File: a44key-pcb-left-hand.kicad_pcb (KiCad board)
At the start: 2 copper layers, 116.7 x 103.9 mm, 69 parts, among them J1 AudioJack3, J2 Conn_01x04_Female, J3 Conn_01x04_Female, J4 Conn_01x04_Female, SW1 SW_Push, U1 ATmega32U4-AU, Y1 16MHz

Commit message: PCB Left Hand Added
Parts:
- moved C7 18.9 mm to (180.3, 127.7)
- moved C6 18.9 mm to (175.0, 127.7)
- moved C9 18.9 mm to (173.0, 127.7)
- moved Right-Left1 18.8 mm to (181.6, 108.9), turned to 270 degrees
- moved R4 18.1 mm to (178.3, 109.1)
- moved C8 16.0 mm to (171.6, 110.5)
- moved R3 10.1 mm to (164.9, 122.9)
- moved R5 8.23 mm to (161.3, 121.8)
- moved C2 7.42 mm to (159.5, 114.2)
- moved F1 6.86 mm to (163.1, 56.6), turned to 90 degrees
- moved C4 6.06 mm to (164.9, 120.9)
- moved Y1 4.86 mm to (163.7, 115.2)
- moved C11 3.94 mm to (182.9, 121.0)
- moved R2 3.05 mm to (158.0, 56.4), turned to 90 degrees
- moved C1 1.82 mm to (182.9, 124.7)
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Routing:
- net COL0: track 0.00 -> 260.3 mm, vias 0 -> 4
- net COL1: track 0.00 -> 233.0 mm, vias 0 -> 2
- net COL2: track 0.00 -> 202.1 mm, vias 0 -> 1
- net COL5: track 0.00 -> 184.6 mm, vias 0 -> 1
- net GND: track 0.00 -> 176.1 mm, vias 0 -> 4
- net COL3: track 0.00 -> 173.1 mm
- net COL4: track 0.00 -> 136.2 mm, vias 0 -> 1
- net VCC: track 0.00 -> 136.1 mm, vias 0 -> 5
- net Net-(R2-Pad1): track 0.00 -> 117.1 mm, vias 0 -> 2
- net Net-(R1-Pad1): track 0.00 -> 112.4 mm, vias 0 -> 2
- net +5V: track 0.00 -> 109.1 mm, vias 0 -> 3
- net ROW1: track 0.00 -> 94.5 mm, vias 0 -> 3
- net TH35: track 0.00 -> 89.1 mm, vias 0 -> 2
- net ROW0: track 0.00 -> 77.9 mm, vias 0 -> 2
- net SCL: track 0.00 -> 76.7 mm, vias 0 -> 2
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
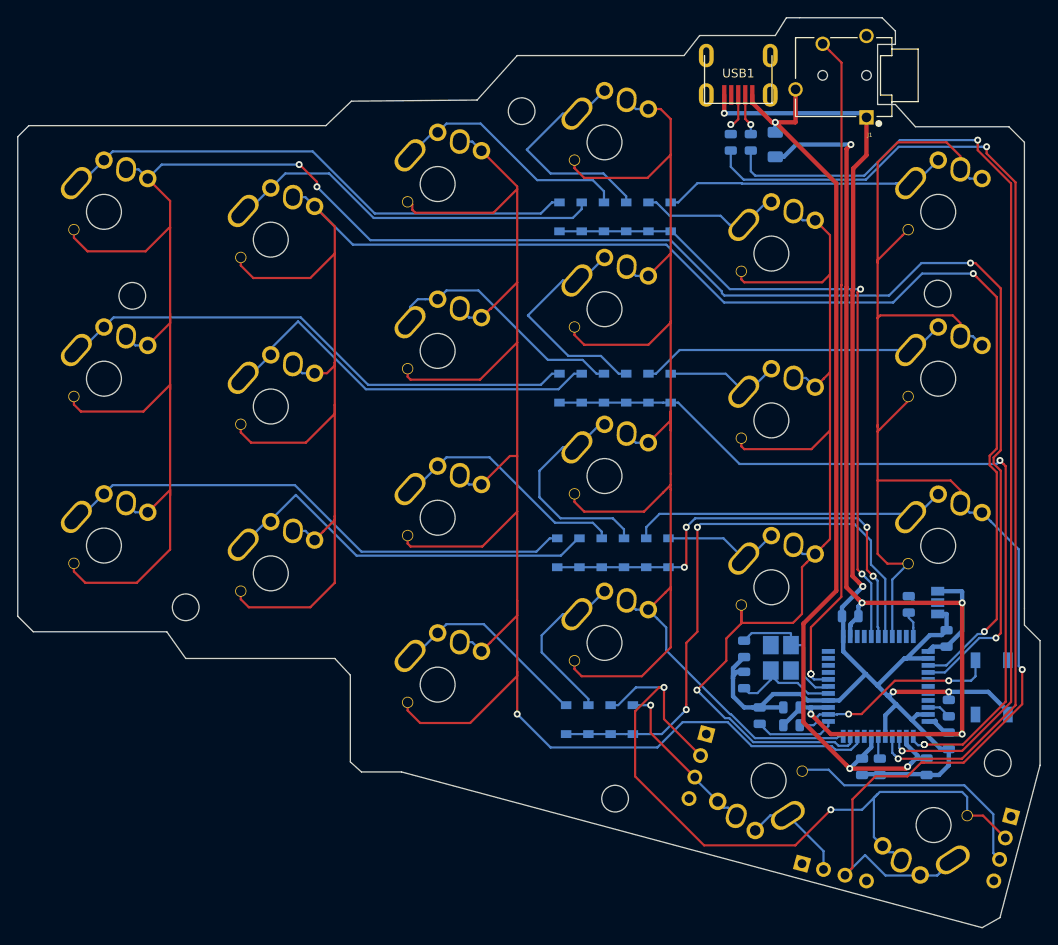
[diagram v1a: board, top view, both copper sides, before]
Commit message: PCB Left Hand Added
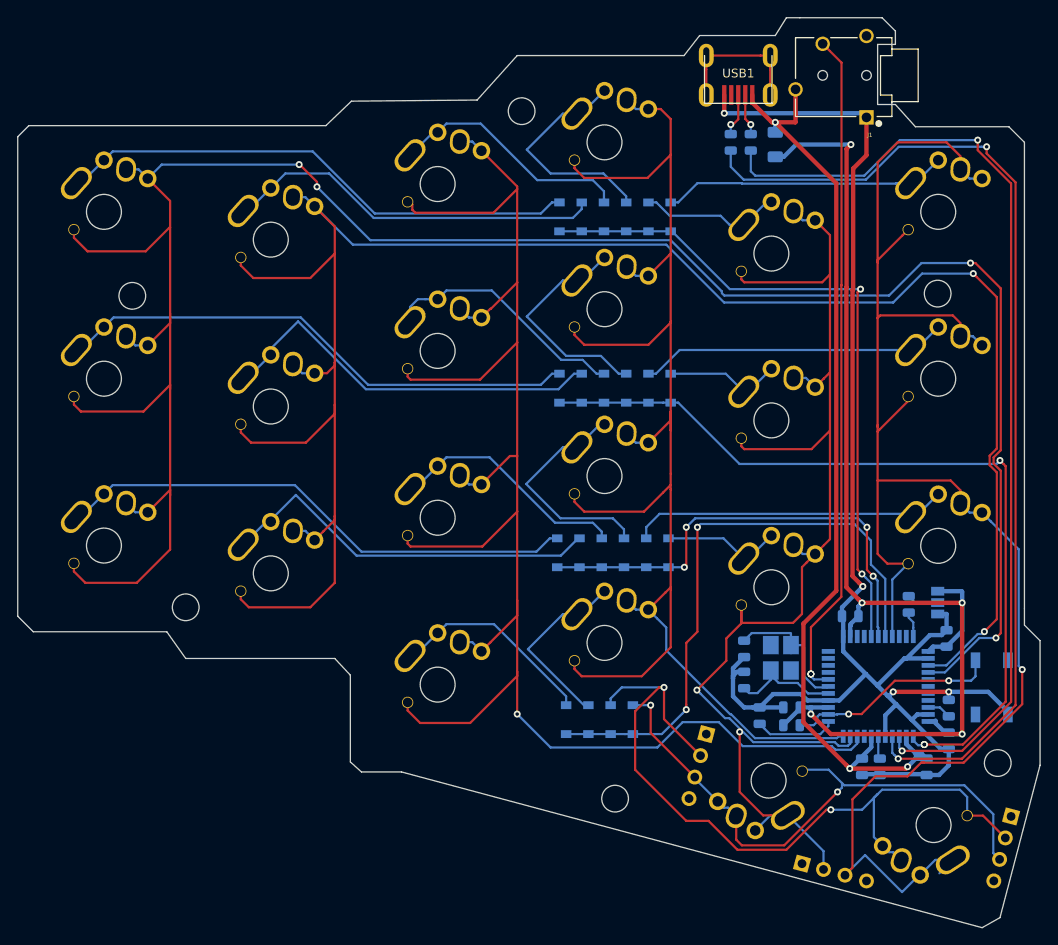
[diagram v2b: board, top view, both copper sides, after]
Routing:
- net TH34: track 48.4 -> 66.7 mm, vias 1 -> 2
- net Net-(USB1-Pad6): track 0.00 -> 16.3 mm
- net COL4: track 136.2 -> 150.0 mm, vias 1 -> 2
- net COL5: track 184.6 -> 188.3 mm
- net +5V: track 109.1 -> 111.3 mm
- net Net-(D12-Pad2): track 19.4 -> 21.0 mm
- net Net-(D11-Pad2): track 24.8 -> 26.1 mm
- net D+: track 3.88 -> 4.97 mm
- net TH35: track 89.1 -> 89.7 mm
- net Net-(D16-Pad2): track 23.2 -> 23.7 mm
